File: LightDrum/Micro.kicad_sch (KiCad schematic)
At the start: 20 parts, among them J1 SWD CONN, SW902 BOOT0, Y32 32.768KHz, Y901 16MHz

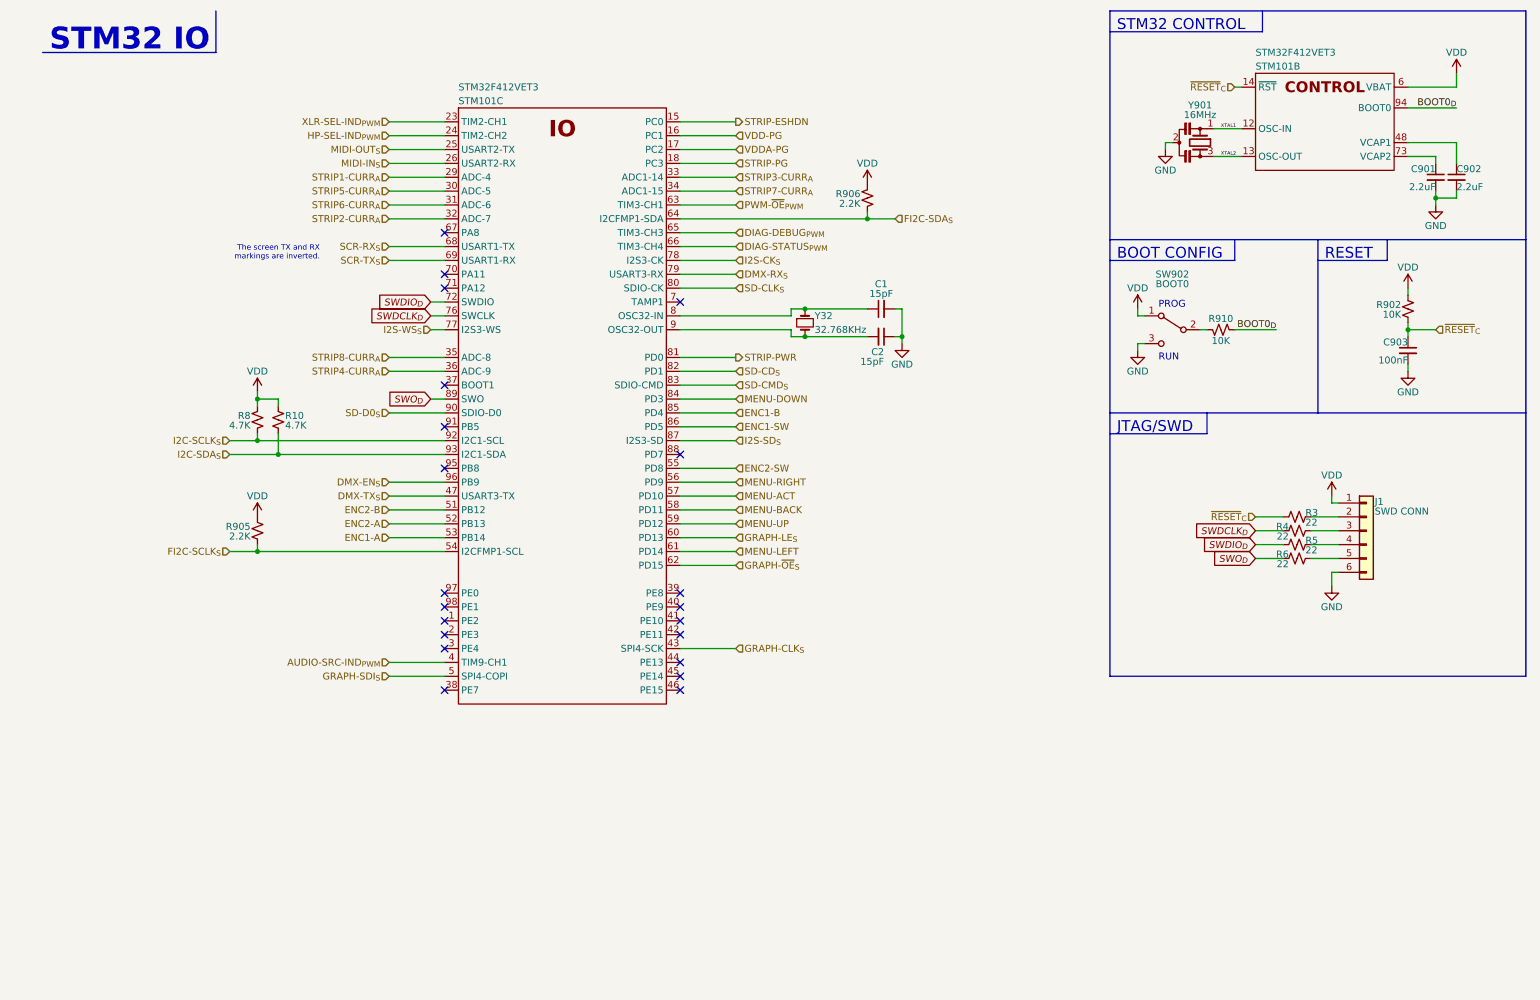
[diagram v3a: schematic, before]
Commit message: Component placement complete
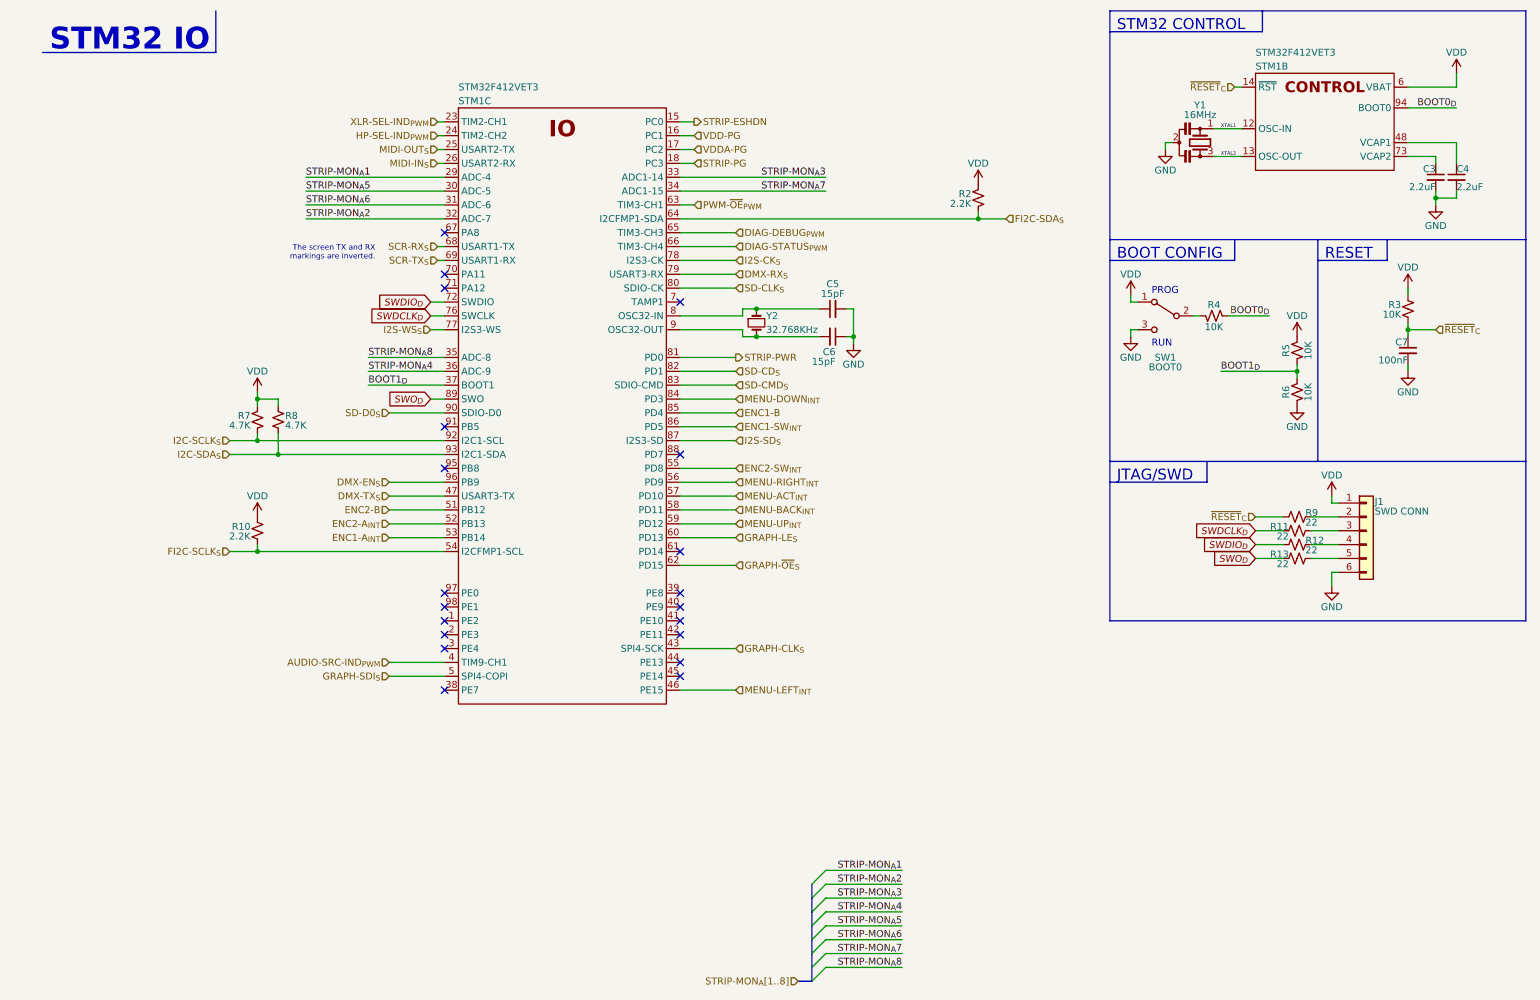
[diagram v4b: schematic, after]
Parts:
- added R5, R6: 10K, Resistor_SMD:R_0402_1005Metric, symbol Device:R_Small_US
- renumbered C901 to C3, C902 to C4, C1 to C5, C2 to C6, C903 to C7, R905 to R10, R4 to R11, R5 to R12, R6 to R13, R906 to R2, R902 to R3, R910 to R4, R8 to R7, R10 to R8, R3 to R9, STM101 to STM1, SW902 to SW1, Y901 to Y1, Y32 to Y2
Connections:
- net GND: now also R6.1
- net VDD: now also R5.2
- net BOOT1_{D}: now reaches STM1.37 (PB2)
- net BOOT1_{D}: now also R5.1, R6.2
- net MENU-LEFT_{INT}: now reaches STM1.46 (PE15)
- net ENC1-A renamed ENC1-A_{INT}
- net ENC1-SW renamed ENC1-SW_{INT}
- net ENC2-A renamed ENC2-A_{INT}
- net ENC2-SW renamed ENC2-SW_{INT}
- net MENU-ACT renamed MENU-ACT_{INT}
- net MENU-BACK renamed MENU-BACK_{INT}
- net MENU-DOWN renamed MENU-DOWN_{INT}
- net MENU-LEFT: no longer names the net of STM1.61 (PD14)
- net MENU-RIGHT renamed MENU-RIGHT_{INT}
- net MENU-UP renamed MENU-UP_{INT}
- net STRIP1-CURR_{A} renamed STRIP-MON_{A}1
- net STRIP2-CURR_{A} renamed STRIP-MON_{A}2
- net STRIP3-CURR_{A} renamed STRIP-MON_{A}3
- net STRIP4-CURR_{A} renamed STRIP-MON_{A}4
- net STRIP5-CURR_{A} renamed STRIP-MON_{A}5
- net STRIP6-CURR_{A} renamed STRIP-MON_{A}6
- net STRIP7-CURR_{A} renamed STRIP-MON_{A}7
- net STRIP8-CURR_{A} renamed STRIP-MON_{A}8
- no-connect marks 21 -> 20
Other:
- moved on the sheet: C5, C6, R2, R4, SW1, Y2

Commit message: First draft layout almost complete
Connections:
- net AUDIO-SRC-IND_{PWM}: now also STM1.67 (PA8); no longer STM1.4 (PE5)
- net ENC1-B: now also STM1.60 (PD13); no longer STM1.85 (PD4)
- net GRAPH-LE_{S}: now also STM1.61 (PD14); no longer STM1.60 (PD13)
- net HP-SEL-IND_{PWM}: now also STM1.23 (PA0); no longer STM1.24 (PA1)
- net STRIP-MON_{A}2: now also STM1.31 (PA6); no longer STM1.32 (PA7)
- net STRIP-MON_{A}3: now also STM1.34 (PC5); no longer STM1.33 (PC4)
- net STRIP-MON_{A}4: now also STM1.35 (PB0); no longer STM1.36 (PB1)
- net STRIP-MON_{A}6: now also STM1.32 (PA7); no longer STM1.31 (PA6)
- net STRIP-MON_{A}7: now also STM1.33 (PC4); no longer STM1.34 (PC5)
- net STRIP-MON_{A}8: now also STM1.36 (PB1); no longer STM1.35 (PB0)
- net XLR-SEL-IND_{PWM}: now also STM1.24 (PA1); no longer STM1.23 (PA0)
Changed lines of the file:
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@@
   (no_connect (at 129.54 124.46))
   (no_connect (at 86.36 88.9))
-  (no_connect (at 86.36 53.34))
+  (no_connect (at 129.54 86.36))
   (no_connect (at 86.36 137.16))
+  (no_connect (at 86.36 132.08))
   (no_connect (at 129.54 119.38))
   (no_connect (at 86.36 121.92))
   (no_connect (at 86.36 60.96))
   (no_connect (at 129.54 134.62))
-  (no_connect (at 129.54 111.76))
   (no_connect (at 129.54 93.98))
   (no_connect (at 86.36 63.5))
@@
     (stroke (width 0) (type default))
   )
-  (wire (pts (xy 139.7 86.36) (xy 129.54 86.36))
+  (wire (pts (xy 139.7 109.22) (xy 129.54 109.22))
     (stroke (width 0) (type default))
   )
@@
     (stroke (width 0) (type default))
   )
-  (wire (pts (xy 76.2 132.08) (xy 86.36 132.08))
+  (wire (pts (xy 76.2 53.34) (xy 86.36 53.34))
     (stroke (width 0) (type default))
   )
@@
     (stroke (width 0) (type default))
   )
-  (wire (pts (xy 139.7 109.22) (xy 129.54 109.22))
+  (wire (pts (xy 139.7 111.76) (xy 129.54 111.76))
     (stroke (width 0) (type default))
   )
@@
     (effects (font (size 1.27 1.27)) (justify left bottom))
   )
-  (label "STRIP-MON_{A}3" (at 156.21 43.18 180) (fields_autoplaced)
+  (label "STRIP-MON_{A}3" (at 156.21 45.72 180) (fields_autoplaced)
     (effects (font (size 1.27 1.27)) (justify right bottom))
   )
@@
     (effects (font (size 0.64 0.64)) (justify left bottom))
   )
-  (label "STRIP-MON_{A}2" (at 60.96 50.8 0) (fields_autoplaced)
+  (label "STRIP-MON_{A}2" (at 60.96 48.26 0) (fields_autoplaced)
     (effects (font (size 1.27 1.27)) (justify left bottom))
   )
-  (label "STRIP-MON_{A}6" (at 60.96 48.26 0) (fields_autoplaced)
+  (label "STRIP-MON_{A}6" (at 60.96 50.8 0) (fields_autoplaced)
     (effects (font (size 1.27 1.27)) (justify left bottom))
   )
-  (label "STRIP-MON_{A}8" (at 72.39 76.2 0) (fields_autoplaced)
+  (label "STRIP-MON_{A}8" (at 72.39 78.74 0) (fields_autoplaced)
     (effects (font (size 1.27 1.27)) (justify left bottom))
   )
-  (label "STRIP-MON_{A}4" (at 72.39 78.74 0) (fields_autoplaced)
+  (label "STRIP-MON_{A}4" (at 72.39 76.2 0) (fields_autoplaced)
     (effects (font (size 1.27 1.27)) (justify left bottom))
   )
@@
     (effects (font (size 1.27 1.27)) (justify right bottom))
   )
-  (label "STRIP-MON_{A}7" (at 156.21 45.72 180) (fields_autoplaced)
+  (label "STRIP-MON_{A}7" (at 156.21 43.18 180) (fields_autoplaced)
     (effects (font (size 1.27 1.27)) (justify right bottom))
   )
@@
     )
   )
-  (hierarchical_label "GRAPH-LE_{S}" (shape input) (at 139.7 109.22 0) (fields_autoplaced)
+  (hierarchical_label "GRAPH-LE_{S}" (shape input) (at 139.7 111.76 0) (fields_autoplaced)
     (effects (font (size 1.27 1.27)) (justify left))
   )
@@
     (effects (font (size 1.27 1.27)) (justify left))
   )
-  (hierarchical_label "AUDIO-SRC-IND_{PWM}" (shape input) (at 76.2 132.08 180) (fields_autoplaced)
+  (hierarchical_label "AUDIO-SRC-IND_{PWM}" (shape input) (at 76.2 53.34 180) (fields_autoplaced)
     (effects (font (size 1.27 1.27)) (justify right))
   )
@@
     (effects (font (size 1.27 1.27)) (justify right))
   )
-  (hierarchical_label "XLR-SEL-IND_{PWM}" (shape input) (at 85.09 33.02 180) (fields_autoplaced)
+  (hierarchical_label "XLR-SEL-IND_{PWM}" (shape input) (at 85.09 35.56 180) (fields_autoplaced)
     (effects (font (size 1.27 1.27)) (justify right))
   )
@@
     (effects (font (size 1.27 1.27)) (justify right))
   )
-  (hierarchical_label "HP-SEL-IND_{PWM}" (shape input) (at 85.09 35.56 180) (fields_autoplaced)
+  (hierarchical_label "HP-SEL-IND_{PWM}" (shape input) (at 85.09 33.02 180) (fields_autoplaced)
     (effects (font (size 1.27 1.27)) (justify right))
   )
@@
     (effects (font (size 1.27 1.27)) (justify left))
   )
-  (hierarchical_label "ENC1-B" (shape input) (at 139.7 86.36 0) (fields_autoplaced)
+  (hierarchical_label "ENC1-B" (shape input) (at 139.7 109.22 0) (fields_autoplaced)
     (effects (font (size 1.27 1.27)) (justify left))
   )
@@
     (pin "38")
     (pin "39")
-    (pin "4" (alternate "TIM9-CH1"))
+    (pin "4")
     (pin "40")
     (pin "41")
@@
     (pin "65" (alternate "TIM3-CH3"))
     (pin "66" (alternate "TIM3-CH4"))
-    (pin "67")
+    (pin "67" (alternate "TIM1-CH1"))
     (pin "68" (alternate "USART1-TX"))
     (pin "69" (alternate "USART1-RX"))
@@
     (pin "38")
     (pin "39")
-    (pin "4" (alternate "TIM9-CH1"))
+    (pin "4")
     (pin "40")
     (pin "41")
@@
     (pin "65" (alternate "TIM3-CH3"))
     (pin "66" (alternate "TIM3-CH4"))
-    (pin "67")
+    (pin "67" (alternate "TIM1-CH1"))
     (pin "68" (alternate "USART1-TX"))
     (pin "69" (alternate "USART1-RX"))

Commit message: PCB Lock REV11
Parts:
- Y2: footprint Crystal:Crystal_SMD_3215-2Pin_3.2x1.5mm -> Daxxn_Passives:Crystal_SMD_3215-2Pin_3.2x1.5mm
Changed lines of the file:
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@@
       (effects (font (size 1.27 1.27)) (justify left))
     )
-    (property "Footprint" "Crystal:Crystal_SMD_3215-2Pin_3.2x1.5mm" (at 143.51 69.85 0)
+    (property "Footprint" "Daxxn_Passives:Crystal_SMD_3215-2Pin_3.2x1.5mm" (at 143.51 69.85 0)
       (effects (font (size 1.27 1.27)) hide)
     )

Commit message: Minor fixes and cleanup - REV11
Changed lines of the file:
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@@
     (stroke (width 0) (type default))
   )
-  (wire (pts (xy 156.21 45.72) (xy 129.54 45.72))
+  (wire (pts (xy 158.75 45.72) (xy 129.54 45.72))
     (stroke (width 0) (type default))
   )
@@
     (stroke (width 0) (type default))
   )
-  (wire (pts (xy 156.21 43.18) (xy 129.54 43.18))
+  (wire (pts (xy 158.75 43.18) (xy 129.54 43.18))
     (stroke (width 0) (type default))
   )
@@
     (effects (font (size 1.27 1.27)) (justify left bottom))
   )
-  (label "STRIP-MON_{A}3" (at 156.21 45.72 180) (fields_autoplaced)
+  (label "STRIP-MON_{A}3" (at 158.75 45.72 180) (fields_autoplaced)
     (effects (font (size 1.27 1.27)) (justify right bottom))
   )
@@
     (effects (font (size 1.27 1.27)) (justify right bottom))
   )
-  (label "STRIP-MON_{A}7" (at 156.21 43.18 180) (fields_autoplaced)
-    (effects (font (size 1.27 1.27)) (justify right bottom))
-  )
+  (label "STRIP-MON_{A}7" (at 158.75 43.18 180) (fields_autoplaced)
+    (effects (font (size 1.27 1.27)) (justify right bottom))
+  )

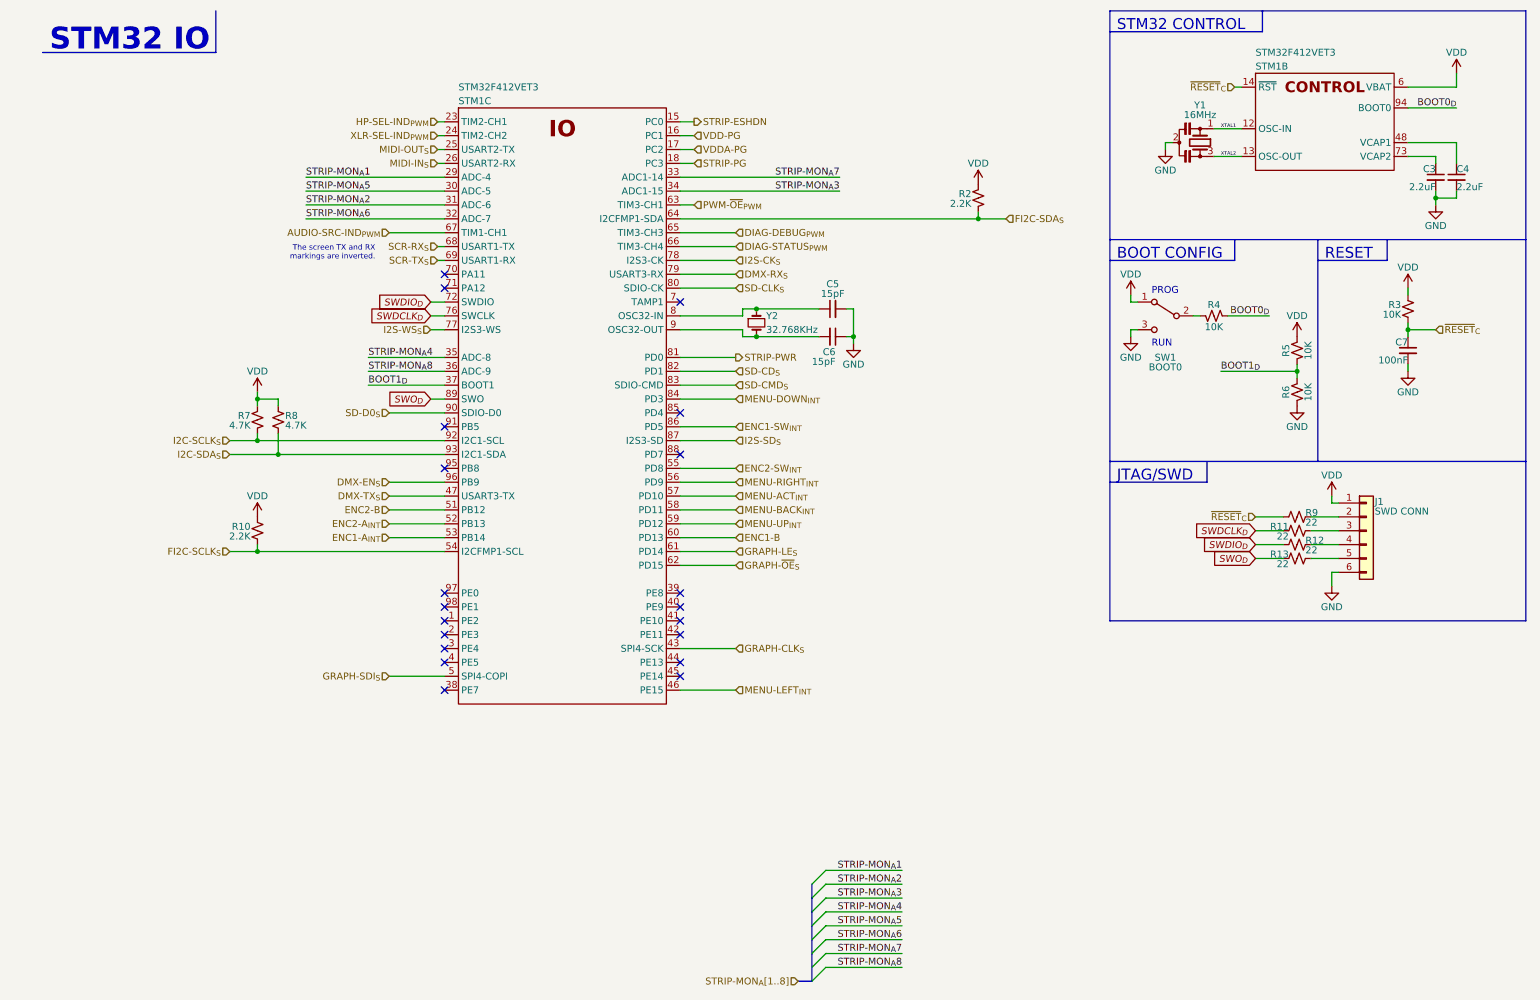
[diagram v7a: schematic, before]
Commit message: replace STM32 package with 100-BGA
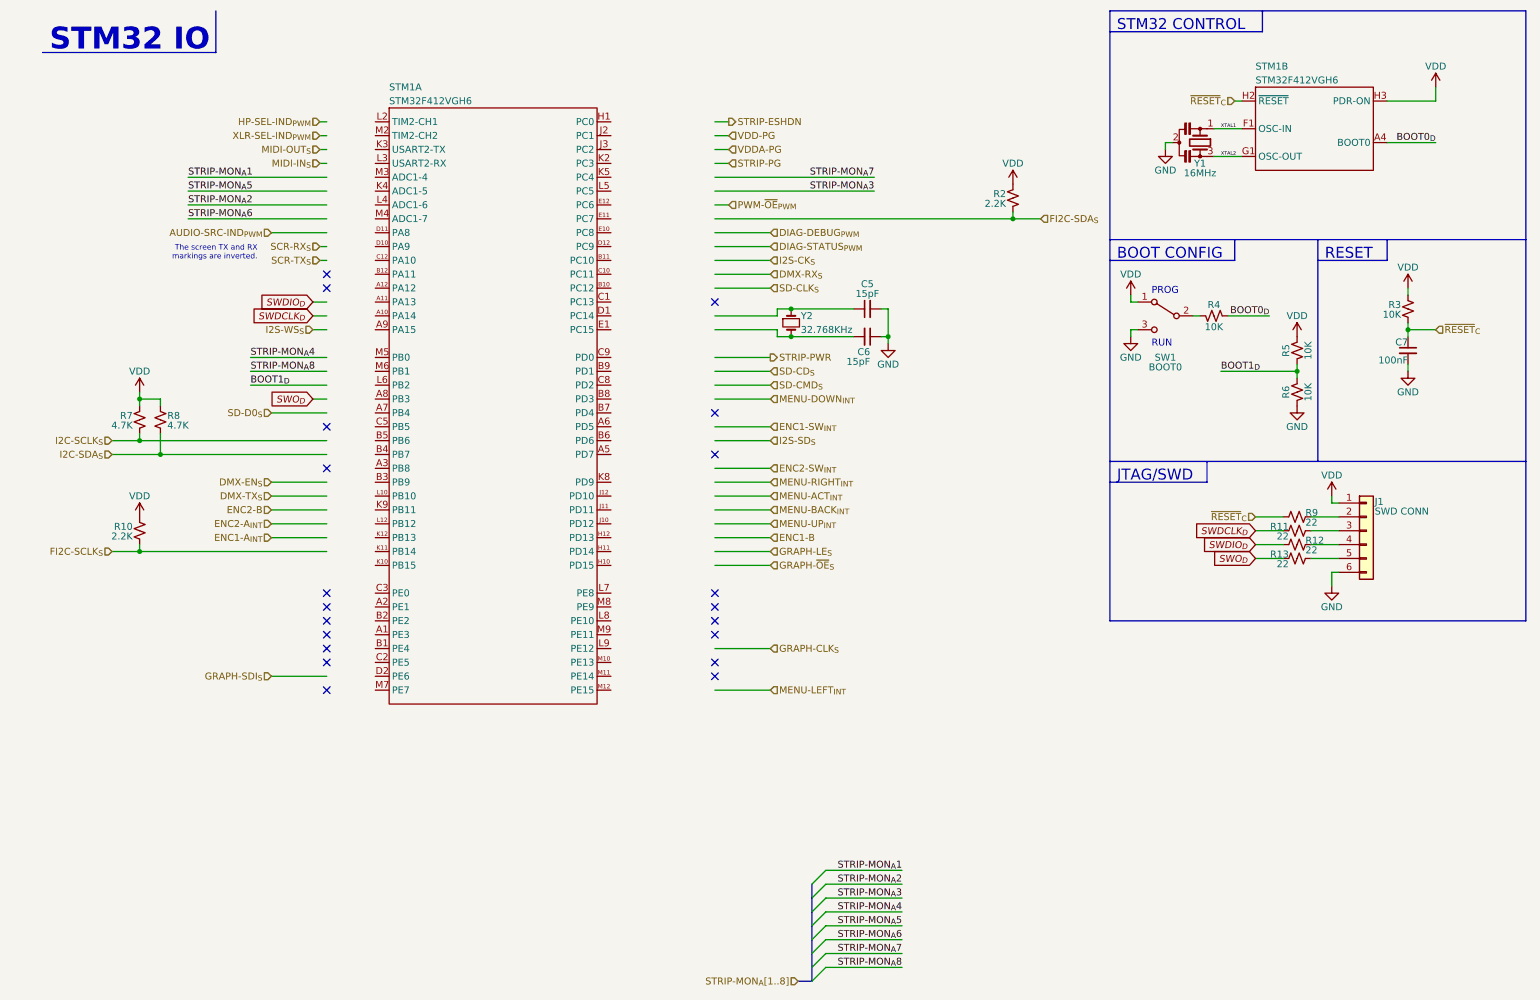
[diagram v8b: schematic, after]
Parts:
- removed C3, C4: 2.2uF, Capacitor_SMD:C_0402_1005Metric, symbol Device:C_Small
- removed STM1: STM32F412VET3, Package_QFP:LQFP-100_14x14mm_P0.5mm, symbol Daxxn_STMicros:STM32F412VET3
- added STM1: STM32F412VGH6, Package_BGA:UFBGA-100_7x7mm_Layout12x12_P0.5mm, symbol Daxxn_STMicros:STM32F412VGH6
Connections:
- net BOOT0_{D}: now also STM1.A4 (BOOT0)
- net VDD: now also STM1.H3 (PDR-ON)
- net XTAL1: now also STM1.F1 (OSC-IN)
- net XTAL2: now also STM1.G1 (OSC-OUT)
- net ~{RESET}_{C}: now also STM1.H2 (~{RESET})
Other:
- moved on the sheet: C5, C6, R10, R2, R7, R8, Y2
